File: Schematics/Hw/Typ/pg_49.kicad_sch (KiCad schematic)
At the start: 55 parts, among them U5101 F169, U5102 F169, U5103 F169, U5104 F169, U5105 F00, U5106 F00, U5107 F00, U5108 F00, U5109 F00, U5110 F00, U5111 F00, U5112 F00, U5113 F00, U5114 F00, U5115 F00, U5116 F00, U5117 F00, U5118 F00, U5119 F37, U5120 F37, U5121 F37, U5122 F37, U5123 F37, U5124 F37, U5125 F37, U5126 F37, U5127 F37, U5128 F37, U5129 F37, U5130 F37, U5131 F37, U5132 F37, U5133 F240, U5134 F240, U5135 F00, U5136 F00, U5137 93S48, U5138 93S48, U5139 F02

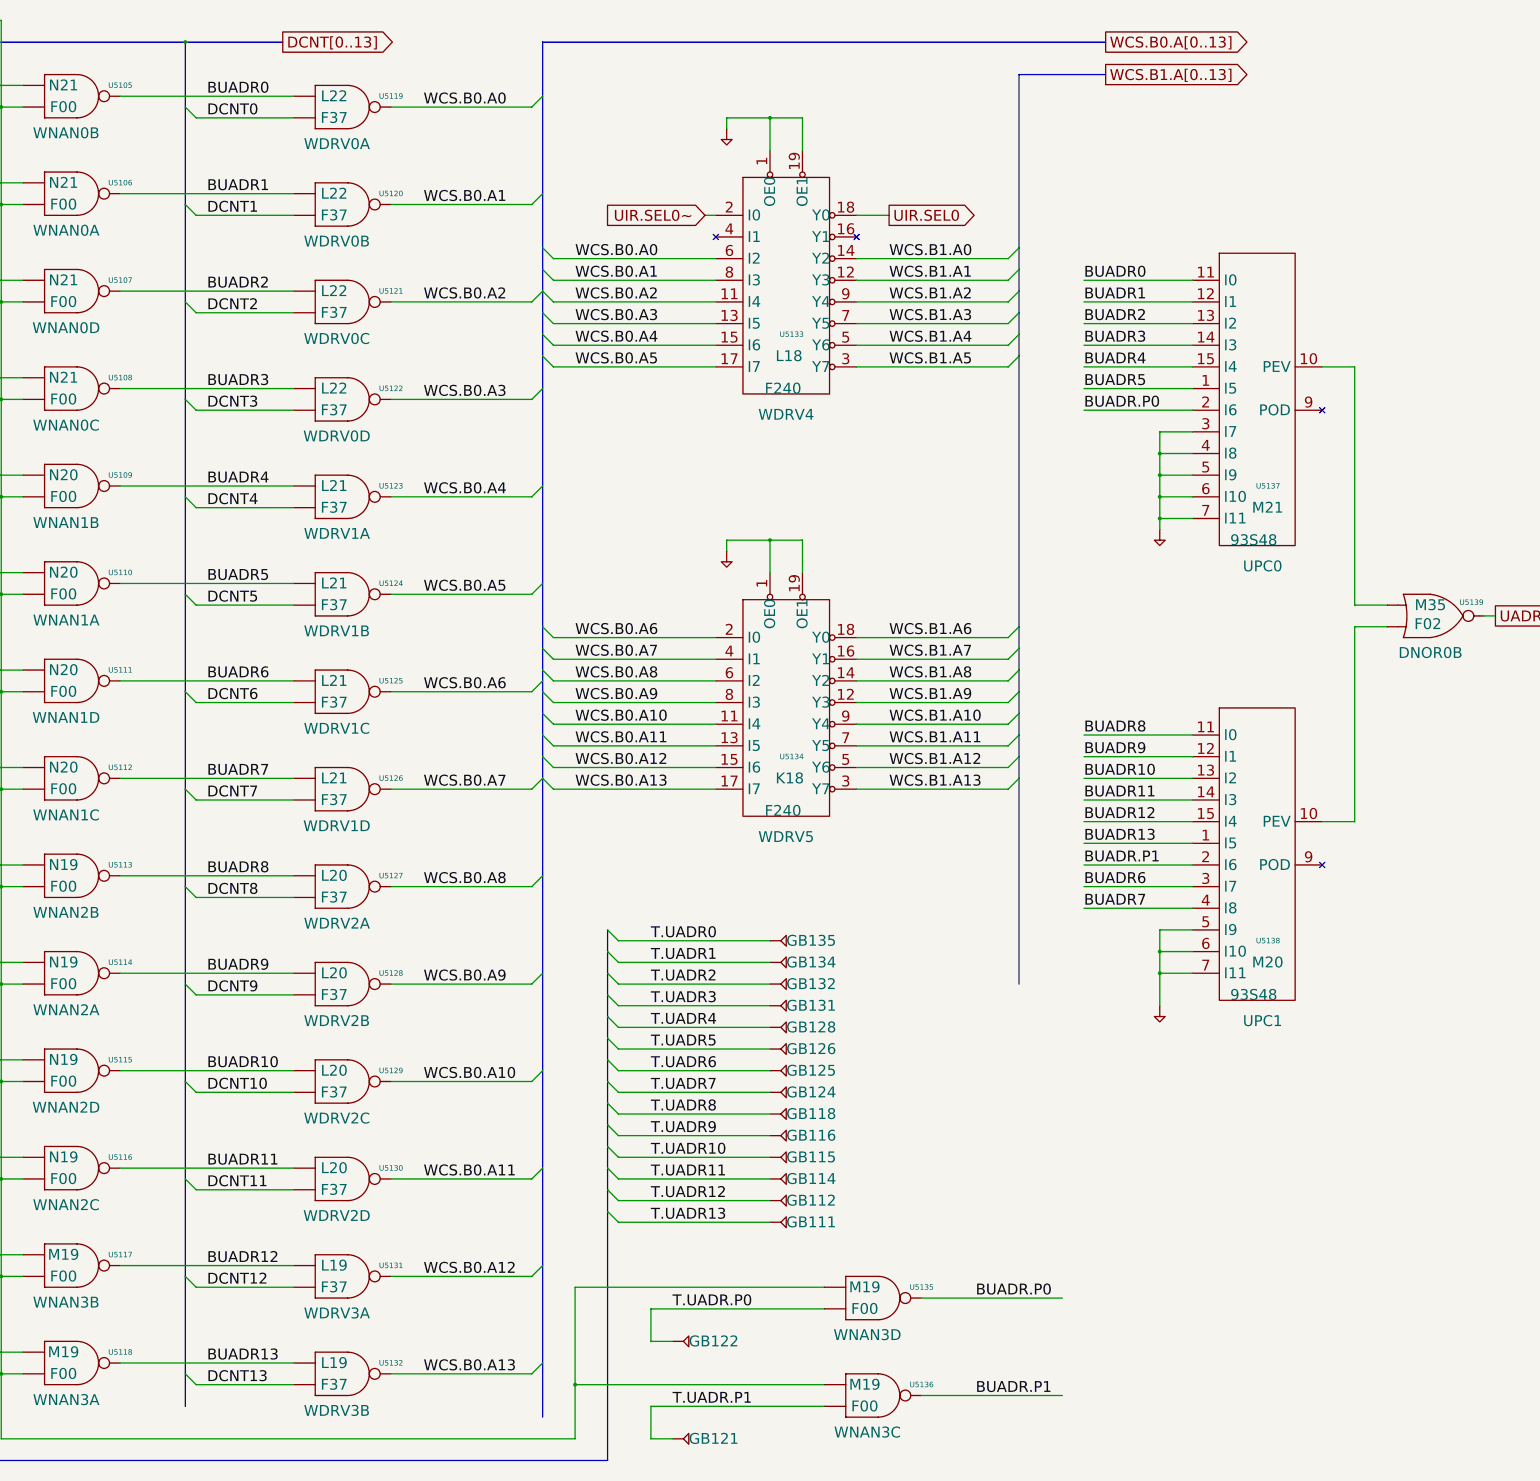
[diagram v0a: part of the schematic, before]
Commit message: Upgrade to KiCad9
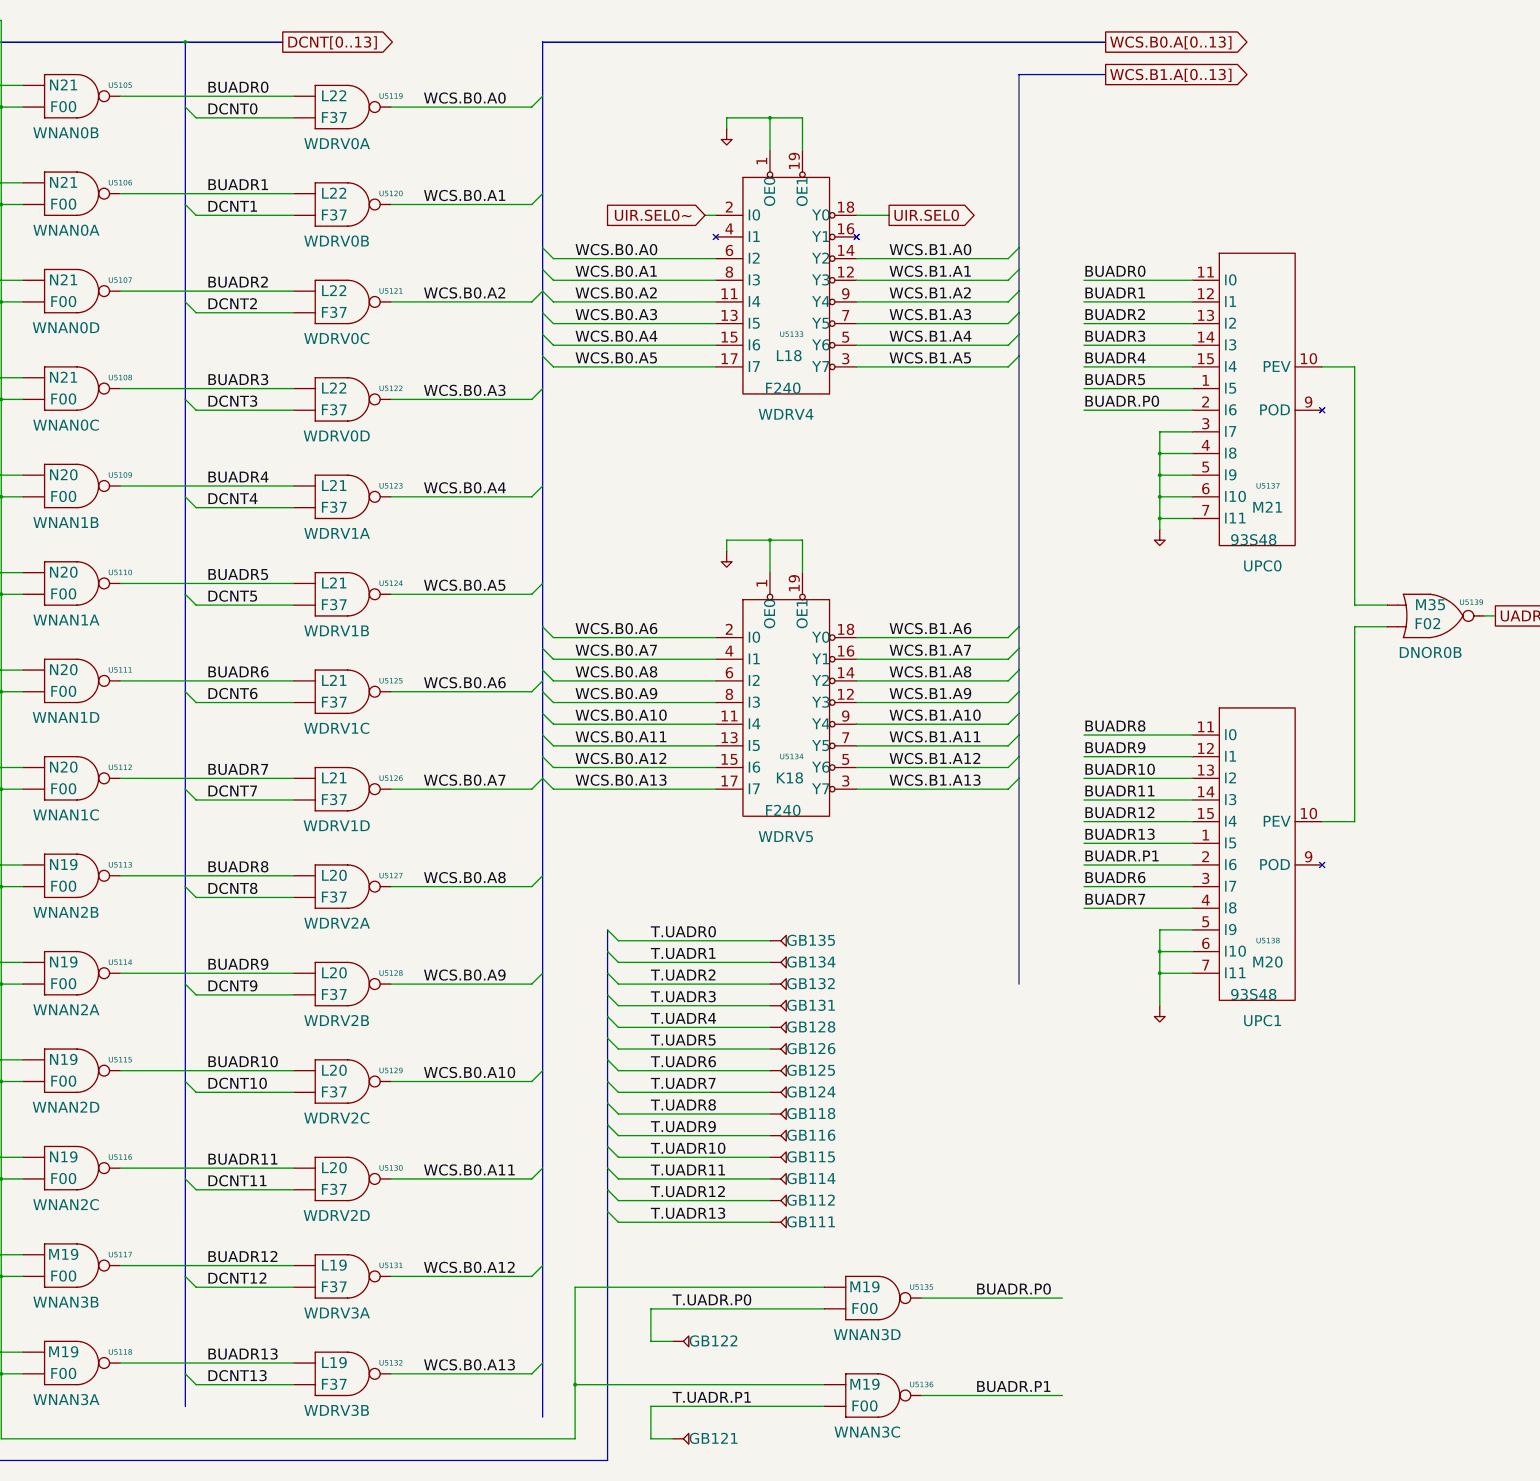
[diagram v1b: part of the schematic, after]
